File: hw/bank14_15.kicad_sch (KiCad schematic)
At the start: 24 parts, among them U2 AT25SL641, U24 XC7A35T-FTG256

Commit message: WIP (layout)
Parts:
- removed R18: 50, Resistor_SMD:R_0603_1608Metric, symbol Device:R_Small
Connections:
- net at U2.2 (SO/SIO1): now also U24.J14 (IO_L1N_T0_D01_DIN_14)
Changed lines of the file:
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@@
-    (stroke (width 0) (type default))
-  )
-  (wire (pts (xy 231.14 90.17) (xy 229.87 90.17))
     (stroke (width 0) (type default))
   )
@@
     (stroke (width 0) (type default))
   )
-  (wire (pts (xy 240.03 90.17) (xy 236.22 90.17))
+  (wire (pts (xy 229.87 90.17) (xy 240.03 90.17))
     (stroke (width 0) (type default))
   )
@@
         )
       )
-    )
-  )
-  (symbol (lib_id "Device:R_Small") (at 233.68 90.17 270) (unit 1)
-    (in_bom yes) (on_board yes) (dnp no)
-    (property "Reference" "R18" (at 237.49 88.9 90)
-      (effects (font (size 1.27 1.27)))
-    )
-    (property "Value" "50" (at 245.11 88.9 90)
-      (effects (font (size 1.27 1.27)))
-    )
-    (property "Footprint" "Resistor_SMD:R_0603_1608Metric" (at 233.68 90.17 0)
-      (effects (font (size 1.27 1.27)) hide)
-    )
-    (property "Datasheet" "~" (at 233.68 90.17 0)
-      (effects (font (size 1.27 1.27)) hide)
-    )
-    (pin "1")
-    (pin "2")
-    (instances
-      (project "ecevr-proto"
-        (path "/0333b818-5fb1-4de6-9929-c91b1fef8666/00000000-0000-0000-0000-0000620d1e32/00000000-0000-0000-0000-0000622d3d90"
-          (reference "R18") (unit 1)
-        )
-      )
-      (project "usbadc"
-        (path "/7c8a1f8d-8834-4c9b-aaae-1f231e9b09a1/27cc8612-21b5-4a6c-80ae-cd0836a5c2c4/3a56c443-70de-4e54-a6cb-56b00baa10da"
-          (reference "R105") (unit 1)
-        )
-      )

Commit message: WIP - a lot already laid out.
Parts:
- JP3: value PUDC_dis -> PUDC
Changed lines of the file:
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@@
       (effects (font (size 1.27 1.27)))
     )
-    (property "Value" "PUDC_dis" (at 151.13 44.45 90)
+    (property "Value" "PUDC" (at 151.13 44.45 90)
       (effects (font (size 1.27 1.27)))
     )

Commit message: layout finished (draft)
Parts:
- JP3: symbol Device:Jumper_NO_Small -> Jumper:Jumper_2_Open
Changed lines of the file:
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@@
   (junction (at 92.71 30.48) (diameter 0) (color 0 0 0 0)
   )
+  (junction (at 143.51 34.29) (diameter 0) (color 0 0 0 0)
+  )
   (junction (at 180.34 34.29) (diameter 0) (color 0 0 0 0)
   )
@@
   (junction (at 69.85 30.48) (diameter 0) (color 0 0 0 0)
   )
-  (junction (at 144.78 34.29) (diameter 0) (color 0 0 0 0)
-  )
   (junction (at 125.73 34.29) (diameter 0) (color 0 0 0 0)
   )
@@
     (stroke (width 0) (type default))
   )
+  (wire (pts (xy 143.51 34.29) (xy 143.51 40.005))
+    (stroke (width 0) (type default))
+  )
   (wire (pts (xy 190.5 39.37) (xy 200.66 39.37))
     (stroke (width 0) (type default))
@@
     (stroke (width 0) (type default))
   )
-  (wire (pts (xy 172.72 48.26) (xy 172.72 67.31))
+  (wire (pts (xy 172.72 50.165) (xy 172.72 67.31))
     (stroke (width 0) (type default))
   )
@@
     (stroke (width 0) (type default))
   )
-  (wire (pts (xy 144.78 48.26) (xy 172.72 48.26))
-    (stroke (width 0) (type default))
-  )
-  (wire (pts (xy 144.78 43.18) (xy 144.78 34.29))
+  (wire (pts (xy 143.51 50.165) (xy 172.72 50.165))
     (stroke (width 0) (type default))
   )
@@
     (stroke (width 0) (type default))
   )
-  (wire (pts (xy 135.89 34.29) (xy 144.78 34.29))
-    (stroke (width 0) (type default))
-  )
   (wire (pts (xy 203.2 78.74) (xy 253.365 78.74))
     (stroke (width 0) (type default))
@@
     (stroke (width 0) (type default))
   )
-  (wire (pts (xy 144.78 34.29) (xy 148.59 34.29))
+  (wire (pts (xy 135.89 34.29) (xy 143.51 34.29))
     (stroke (width 0) (type default))
   )
@@
   )
   (wire (pts (xy 200.66 71.12) (xy 196.85 71.12))
+    (stroke (width 0) (type default))
+  )
+  (wire (pts (xy 143.51 34.29) (xy 148.59 34.29))
     (stroke (width 0) (type default))
   )
@@
     )
   )
-  (symbol (lib_id "Device:Jumper_NO_Small") (at 144.78 45.72 270) (unit 1)
-    (in_bom yes) (on_board yes) (dnp no)
-    (property "Reference" "JP3" (at 148.59 46.99 90)
-      (effects (font (size 1.27 1.27)))
-    )
-    (property "Value" "PUDC" (at 151.13 44.45 90)
-      (effects (font (size 1.27 1.27)))
-    )
-    (property "Footprint" "Connector_PinHeader_2.54mm:PinHeader_1x02_P2.54mm_Vertical" (at 144.78 45.72 0)
-      (effects (font (size 1.27 1.27)) hide)
-    )
-    (property "Datasheet" "~" (at 144.78 45.72 0)
-      (effects (font (size 1.27 1.27)) hide)
-    )
+  (symbol (lib_id "Jumper:Jumper_2_Open") (at 143.51 45.085 270) (unit 1)
+    (in_bom yes) (on_board yes) (dnp no)
+    (property "Reference" "JP3" (at 147.32 46.355 90)
+      (effects (font (size 1.27 1.27)))
+    )
+    (property "Value" "PUDC" (at 149.86 43.815 90)
+      (effects (font (size 1.27 1.27)))
+    )
+    (property "Footprint" "Connector_PinHeader_2.54mm:PinHeader_1x02_P2.54mm_Vertical" (at 143.51 45.085 0)
+      (effects (font (size 1.27 1.27)) hide)
+    )
+    (property "Datasheet" "~" (at 143.51 45.085 0)
+      (effects (font (size 1.27 1.27)) hide)
+    )

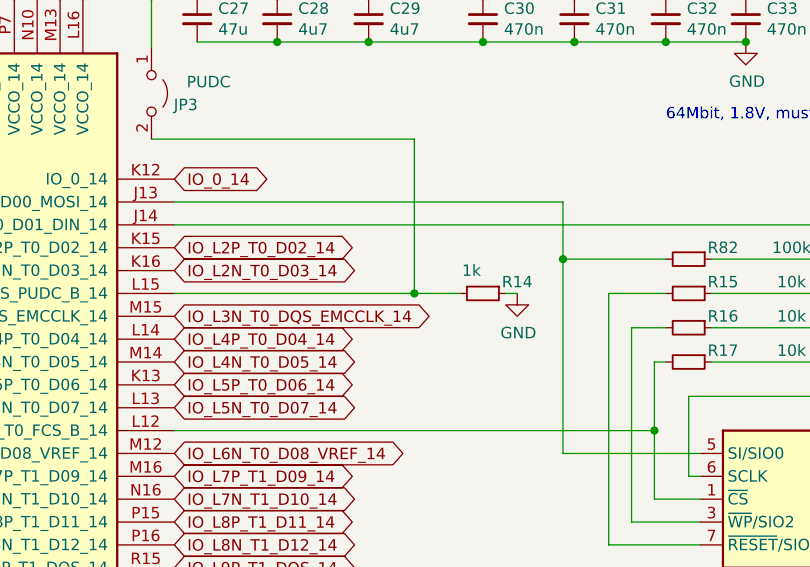
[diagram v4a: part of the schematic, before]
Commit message: added 2nd front led; more keepouts around signal lines
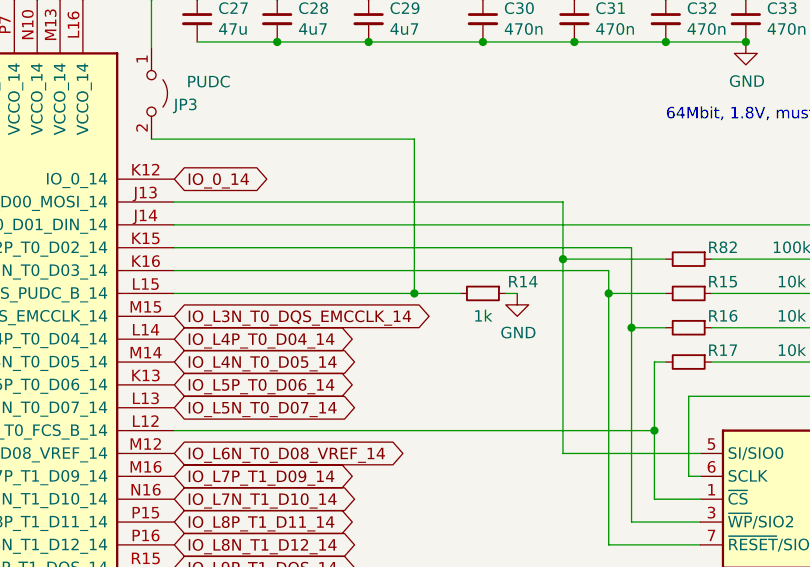
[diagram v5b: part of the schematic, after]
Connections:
- net IO_L2N_T0_D03_14 is gone; now on an unnamed net: U24.K16 (IO_L2N_T0_D03_14)
- net IO_L2P_T0_D02_14 is gone; now on an unnamed net: U24.K15 (IO_L2P_T0_D02_14)
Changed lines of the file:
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@@
 (kicad_sch (version 20230121) (generator eeschema)
   (paper "A4")
+  (junction (at 196.85 71.12) (diameter 0) (color 0 0 0 0)
+  )
   (junction (at 92.71 30.48) (diameter 0) (color 0 0 0 0)
   )
@@
   (junction (at 69.85 30.48) (diameter 0) (color 0 0 0 0)
   )
+  (junction (at 194.31 67.31) (diameter 0) (color 0 0 0 0)
+  )
   (junction (at 125.73 34.29) (diameter 0) (color 0 0 0 0)
   )
@@
     (stroke (width 0) (type default))
   )
+  (wire (pts (xy 196.85 62.23) (xy 196.85 71.12))
+    (stroke (width 0) (type default))
+  )
   (wire (pts (xy 240.03 59.69) (xy 240.03 90.17))
     (stroke (width 0) (type default))
   )
+  (wire (pts (xy 194.31 64.77) (xy 194.31 67.31))
+    (stroke (width 0) (type default))
+  )
   (wire (pts (xy 189.23 63.5) (xy 189.23 85.09))
     (stroke (width 0) (type default))
@@
     (stroke (width 0) (type default))
   )
+  (wire (pts (xy 146.05 62.23) (xy 196.85 62.23))
+    (stroke (width 0) (type default))
+  )
   (wire (pts (xy 172.72 50.165) (xy 172.72 67.31))
     (stroke (width 0) (type default))
@@
   )
   (wire (pts (xy 167.64 39.37) (xy 157.48 39.37))
+    (stroke (width 0) (type default))
+  )
+  (wire (pts (xy 146.05 64.77) (xy 194.31 64.77))
     (stroke (width 0) (type default))
   )
@@
     )
   )
-  (global_label "IO_L2N_T0_D03_14" (shape bidirectional) (at 146.05 64.77 0) (fields_autoplaced)
-    (effects (font (size 1.27 1.27)) (justify left))
-    (property "Intersheetrefs" "${INTERSHEET_REFS}" (at 166.913 64.77 0)
-      (effects (font (size 1.27 1.27)) (justify left) hide)
-    )
-  )
   (global_label "IO_25_15" (shape bidirectional) (at 44.45 179.07 180) (fields_autoplaced)
     (effects (font (size 1.27 1.27)) (justify right))
@@
     (property "Intersheetrefs" "${INTERSHEET_REFS}" (at 21.047 110.49 0)
       (effects (font (size 1.27 1.27)) (justify right) hide)
-    )
-  )
-  (global_label "IO_L2P_T0_D02_14" (shape bidirectional) (at 146.05 62.23 0) (fields_autoplaced)
-    (effects (font (size 1.27 1.27)) (justify left))
-    (property "Intersheetrefs" "${INTERSHEET_REFS}" (at 166.8525 62.23 0)
-      (effects (font (size 1.27 1.27)) (justify left) hide)
     )
   )
@@
   (symbol (lib_id "Device:R_Small") (at 180.34 67.31 270) (unit 1)
     (in_bom yes) (on_board yes) (dnp no)
-    (property "Reference" "R14" (at 184.15 66.04 90)
-      (effects (font (size 1.27 1.27)))
-    )
-    (property "Value" "1k" (at 179.07 64.77 90)
-      (effects (font (size 1.27 1.27)))
-    )
+    (property "Reference" "R14" (at 184.785 66.04 90)
+      (effects (font (size 1.27 1.27)))
+    )
+    (property "Value" "1k" (at 180.34 69.85 90)
+      (effects (font (size 1.27 1.27)))
+    )
